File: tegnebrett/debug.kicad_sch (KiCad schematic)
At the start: 28 parts, among them J6 FPGA_Header_Pin, J9 FPGA_debug1, U1 XC7A100T-2FTG256I, U2 Oscillator 100MHz, U8 IS66WVH16M8DBLL-100B1LI1

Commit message: feat: add footprint for each capacitor
It's all 0805, 1206 or 1210 hand soldering variants.
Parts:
- C46, C47, C48, C49, C50, C51: footprint (none) -> Capacitor_SMD:C_0805_2012Metric_Pad1.18x1.45mm_HandSolder
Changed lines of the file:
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@@
 			)
 		)
-		(property "Footprint" ""
+		(property "Footprint" "Capacitor_SMD:C_0805_2012Metric_Pad1.18x1.45mm_HandSolder"
 			(at 133.0452 41.91 0)
 			(effects
@@
 			)
 		)
-		(property "Footprint" ""
+		(property "Footprint" "Capacitor_SMD:C_0805_2012Metric_Pad1.18x1.45mm_HandSolder"
 			(at 367.9952 85.09 0)
 			(effects
@@
 			)
 		)
-		(property "Footprint" ""
+		(property "Footprint" "Capacitor_SMD:C_0805_2012Metric_Pad1.18x1.45mm_HandSolder"
 			(at 63.1952 30.48 0)
 			(effects
@@
 			)
 		)
-		(property "Footprint" ""
+		(property "Footprint" "Capacitor_SMD:C_0805_2012Metric_Pad1.18x1.45mm_HandSolder"
 			(at 359.1052 85.09 0)
 			(effects
@@
 			)
 		)
-		(property "Footprint" ""
+		(property "Footprint" "Capacitor_SMD:C_0805_2012Metric_Pad1.18x1.45mm_HandSolder"
 			(at 375.6152 85.09 0)
 			(effects
@@
 			)
 		)
-		(property "Footprint" ""
+		(property "Footprint" "Capacitor_SMD:C_0805_2012Metric_Pad1.18x1.45mm_HandSolder"
 			(at 186.3852 138.43 0)
 			(effects

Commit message: feat: add footprint to resistors
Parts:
- R1, R2, R22, R3, R4, R5, R6, R64, R7, R8: footprint (none) -> Resistor_SMD:R_0805_2012Metric_Pad1.20x1.40mm_HandSolder
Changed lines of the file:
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@@
 			)
 		)
-		(property "Footprint" ""
+		(property "Footprint" "Resistor_SMD:R_0805_2012Metric_Pad1.20x1.40mm_HandSolder"
 			(at 120.142 74.93 90)
 			(effects
@@
 			)
 		)
-		(property "Footprint" ""
+		(property "Footprint" "Resistor_SMD:R_0805_2012Metric_Pad1.20x1.40mm_HandSolder"
 			(at 93.218 22.86 90)
 			(effects
@@
 			)
 		)
-		(property "Footprint" ""
+		(property "Footprint" "Resistor_SMD:R_0805_2012Metric_Pad1.20x1.40mm_HandSolder"
 			(at 207.772 175.26 90)
 			(effects
@@
 			)
 		)
-		(property "Footprint" ""
+		(property "Footprint" "Resistor_SMD:R_0805_2012Metric_Pad1.20x1.40mm_HandSolder"
 			(at 143.002 38.1 90)
 			(effects
@@
 			)
 		)
-		(property "Footprint" ""
+		(property "Footprint" "Resistor_SMD:R_0805_2012Metric_Pad1.20x1.40mm_HandSolder"
 			(at 113.792 74.93 90)
 			(effects
@@
 			)
 		)
-		(property "Footprint" ""
+		(property "Footprint" "Resistor_SMD:R_0805_2012Metric_Pad1.20x1.40mm_HandSolder"
 			(at 86.868 22.86 90)
 			(effects
@@
 			)
 		)
-		(property "Footprint" ""
+		(property "Footprint" "Resistor_SMD:R_0805_2012Metric_Pad1.20x1.40mm_HandSolder"
 			(at 174.752 38.1 90)
 			(effects
@@
 			)
 		)
-		(property "Footprint" ""
+		(property "Footprint" "Resistor_SMD:R_0805_2012Metric_Pad1.20x1.40mm_HandSolder"
 			(at 106.172 74.93 90)
 			(effects
@@
 			)
 		)
-		(property "Footprint" ""
+		(property "Footprint" "Resistor_SMD:R_0805_2012Metric_Pad1.20x1.40mm_HandSolder"
 			(at 200.152 175.26 90)
 			(effects
@@
 			)
 		)
-		(property "Footprint" ""
+		(property "Footprint" "Resistor_SMD:R_0805_2012Metric_Pad1.20x1.40mm_HandSolder"
 			(at 181.102 38.1 90)
 			(effects

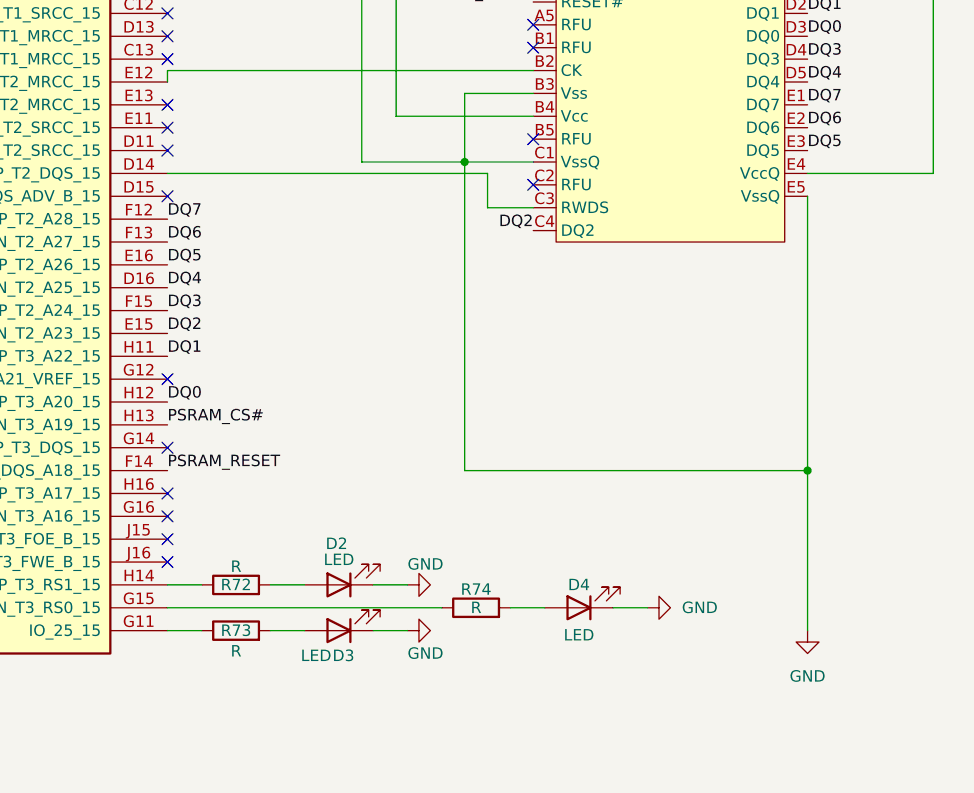
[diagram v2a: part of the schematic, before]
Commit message: refactor: remove some general bottuns from MCU
We have gone down from 9 buttons total to 6 buttons total.
One button is connected to the FPGA.
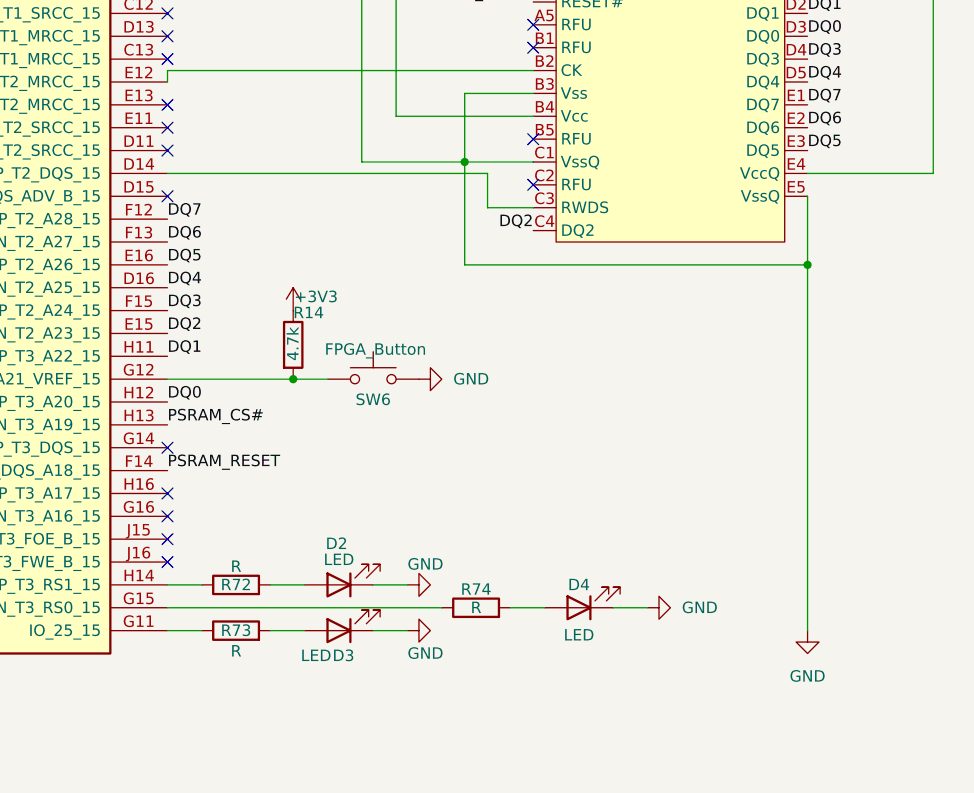
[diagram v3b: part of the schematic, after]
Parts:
- added R14: 4.7k, Resistor_SMD:R_0805_2012Metric_Pad1.20x1.40mm_HandSolder, symbol Device:R
- added SW6: FPGA_Button, symbol Switch:SW_Push
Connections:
- net +3V3: now also R14.1
- net GND: now also SW6.2
- net at U1.G12 (IO_L19N_T3_A21_VREF_15): now also R14.2, SW6.1
- no-connect marks 133 -> 132

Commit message: feat: add footprint to FPGA_debug
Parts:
- J9: footprint (none) -> Connector_PinHeader_2.54mm:PinHeader_2x07_P2.54mm_Vertical
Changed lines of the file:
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@@
 			)
 		)
-		(property "Footprint" ""
+		(property "Footprint" "Connector_PinHeader_2.54mm:PinHeader_2x07_P2.54mm_Vertical"
 			(at 106.68 21.59 0)
 			(effects

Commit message: feat: add and import footprints of trash buttons
These buttons are cheap and do the job fine.
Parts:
- SW6: footprint (none) -> tegnebrett_modules:SW_PS1024ALRED
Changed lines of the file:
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@@
 			)
 		)
-		(property "Footprint" ""
+		(property "Footprint" "tegnebrett_modules:SW_PS1024ALRED"
 			(at 342.9 139.7 0)
 			(effects

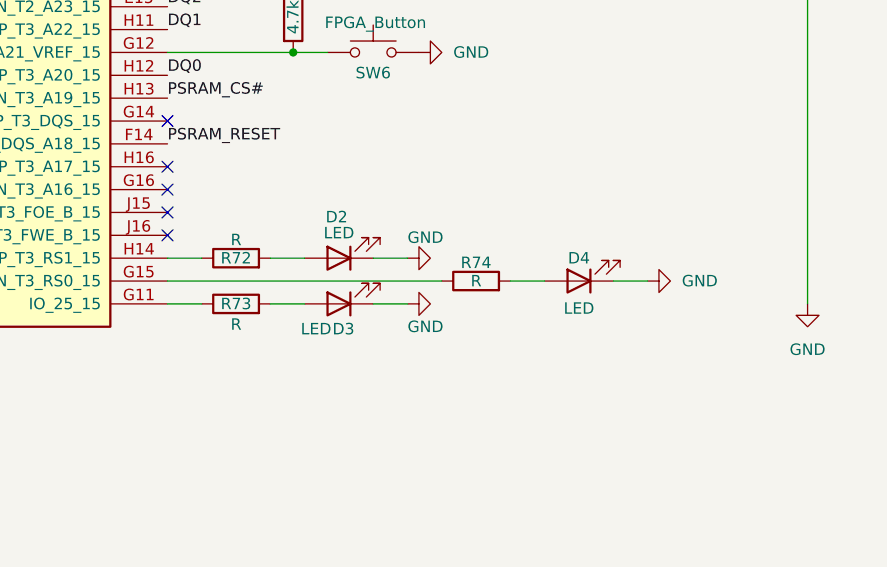
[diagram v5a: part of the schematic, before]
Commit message: refactor: remove unused LEDs
We have too many LEDs.
We're thinking two LEDs for the MCU and two LEDs for the FPGA.
Additionally have one Green LED at power supply to indicate that power
is on.
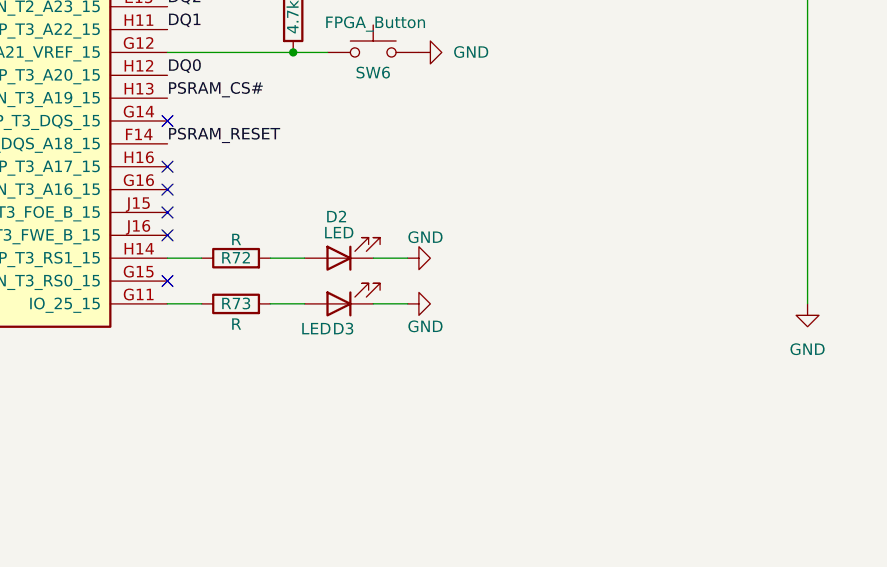
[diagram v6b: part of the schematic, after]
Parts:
- removed D4: LED, tegnebrett_modules:LED_J-SERIES_3030_CRW-M, symbol Device:LED
- removed R74: R, symbol Device:R
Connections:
- no-connect marks 132 -> 133
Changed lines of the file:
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@@
 	)
 	(no_connect
+		(at 320.04 170.18)
+	)
+	(no_connect
 		(at 218.44 106.68)
 	)
@@
 	(wire
 		(pts
-			(xy 369.57 170.18) (xy 373.38 170.18)
-		)
-		(stroke
-			(width 0)
-			(type default)
-		)
-	)
-	(wire
-		(pts
 			(xy 358.14 85.09) (xy 367.03 85.09)
 		)
@@
 	(wire
 		(pts
-			(xy 358.14 170.18) (xy 361.95 170.18)
-		)
-		(stroke
-			(width 0)
-			(type default)
-		)
-	)
-	(wire
-		(pts
 			(xy 100.33 132.08) (xy 102.87 132.08)
 		)
@@
 	(wire
 		(pts
-			(xy 320.04 170.18) (xy 350.52 170.18)
-		)
-		(stroke
-			(width 0)
-			(type default)
-		)
-	)
-	(wire
-		(pts
 			(xy 88.9 34.29) (xy 101.6 34.29)
 		)
@@
 	)
 	(symbol
-		(lib_id "Device:LED")
-		(at 365.76 170.18 180)
-		(unit 1)
-		(exclude_from_sim no)
-		(in_bom yes)
-		(on_board yes)
-		(dnp no)
-		(property "Reference" "D4"
-			(at 365.76 167.64 0)
-			(effects
-				(font
-					(size 1.27 1.27)
-				)
-			)
-		)
-		(property "Value" "LED"
-			(at 365.76 173.228 0)
-			(effects
-				(font
-					(size 1.27 1.27)
-				)
-			)
-		)
-		(property "Footprint" "tegnebrett_modules:LED_J-SERIES_3030_CRW-M"
-			(at 365.76 170.18 0)
-			(effects
-				(font
-					(size 1.27 1.27)
-				)
-				(hide yes)
-			)
-		)
-		(property "Datasheet" "~"
-			(at 365.76 170.18 0)
-			(effects
-				(font
-					(size 1.27 1.27)
-				)
-				(hide yes)
-			)
-		)
-		(property "Description" "Light emitting diode"
-			(at 365.76 170.18 0)
-			(effects
-				(font
-					(size 1.27 1.27)
-				)
-				(hide yes)
-			)
-		)
-		(property "Sim.Pins" "1=K 2=A"
-			(at 365.76 170.18 0)
-			(effects
-				(font
-					(size 1.27 1.27)
-				)
-				(hide yes)
-			)
-		)
-		(pin "2"
-		)
-		(pin "1"
-		)
-		(instances
-			(project "getting-started"
-				(path "/d9a31669-c5f1-42a7-9461-3df04b9a4e62/5e0df967-c6b5-4cdf-8fe6-93251df44e99"
-					(reference "D4")
-					(unit 1)
-				)
-			)
-		)
-	)
-	(symbol
 		(lib_id "power:GND")
 		(at 113.03 132.08 0)
@@
 	(symbol
 		(lib_id "Device:R")
-		(at 354.33 170.18 90)
-		(unit 1)
-		(exclude_from_sim no)
-		(in_bom yes)
-		(on_board yes)
-		(dnp no)
-		(property "Reference" "R74"
-			(at 354.33 168.148 90)
-			(effects
-				(font
-					(size 1.27 1.27)
-				)
-			)
-		)
-		(property "Value" "R"
-			(at 354.33 170.18 90)
-			(effects
-				(font
-					(size 1.27 1.27)
-				)
-			)
-		)
-		(property "Footprint" ""
-			(at 354.33 171.958 90)
-			(effects
-				(font
-					(size 1.27 1.27)
-				)
-				(hide yes)
-			)
-		)
-		(property "Datasheet" "~"
-			(at 354.33 170.18 0)
-			(effects
-				(font
-					(size 1.27 1.27)
-				)
-				(hide yes)
-			)
-		)
-		(property "Description" "Resistor"
-			(at 354.33 170.18 0)
-			(effects
-				(font
-					(size 1.27 1.27)
-				)
-				(hide yes)
-			)
-		)
-		(pin "1"
-		)
-		(pin "2"
-		)
-		(instances
-			(project "getting-started"
-				(path "/d9a31669-c5f1-42a7-9461-3df04b9a4e62/5e0df967-c6b5-4cdf-8fe6-93251df44e99"
-					(reference "R74")
-					(unit 1)
-				)
-			)
-		)
-	)
-	(symbol
-		(lib_id "Device:R")
 		(at 85.09 22.86 180)
 		(unit 1)
@@
 					(unit 1)
 				)
-			)
-		)
-	)
-	(symbol
-		(lib_id "power:GND")
-		(at 373.38 170.18 90)
-		(unit 1)
-		(exclude_from_sim no)
-		(in_bom yes)
-		(on_board yes)
-		(dnp no)
-		(fields_autoplaced yes)
-		(property "Reference" "#PWR084"
-			(at 379.73 170.18 0)
-			(effects
-				(font
-					(size 1.27 1.27)
-				)
-				(hide yes)
-			)
-		)
-		(property "Value" "GND"
-			(at 377.19 170.1799 90)
-			(effects
-				(font
-					(size 1.27 1.27)
-				)
-				(justify right)
-			)
-		)
-		(property "Footprint" ""
-			(at 373.38 170.18 0)
-			(effects
-				(font
-					(size 1.27 1.27)
-				)
-				(hide yes)
-			)
-		)
-		(property "Datasheet" ""
-			(at 373.38 170.18 0)
-			(effects
-				(font
-					(size 1.27 1.27)
-				)
-				(hide yes)
-			)
-		)
-		(property "Description" "Power symbol creates a global label with name \"GND\" , ground"
-			(at 373.38 170.18 0)
-			(effects
-				(font
-					(size 1.27 1.27)
-				)
-				(hide yes)
-			)
-		)
-		(pin "1"
-		)
-		(instances
-			(project "getting-started"
-				(path "/d9a31669-c5f1-42a7-9461-3df04b9a4e62/5e0df967-c6b5-4cdf-8fe6-93251df44e99"
-					(reference "#PWR084")
-					(unit 1)
-				)

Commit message: refactor: use new LED variants.
These have a supply voltage of 2V, and they have a current of 5mA.
These are nice numbers which gives a required resistance of 260 Ohm,
assuming a supply voltage of 3.3V

We're using 270 Ohms though, as 260 is not standard.
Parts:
- D2, D3: footprint tegnebrett_modules:LED_J-SERIES_3030_CRW-M -> tegnebrett_modules:LED_LTST-C193KGKT-5A_LTO-M
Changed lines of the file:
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@@
 			)
 		)
-		(property "Footprint" "tegnebrett_modules:LED_J-SERIES_3030_CRW-M"
+		(property "Footprint" "tegnebrett_modules:LED_LTST-C193KGKT-5A_LTO-M"
 			(at 339.09 167.64 0)
 			(effects
@@
 			)
 		)
-		(property "Footprint" "tegnebrett_modules:LED_J-SERIES_3030_CRW-M"
+		(property "Footprint" "tegnebrett_modules:LED_LTST-C193KGKT-5A_LTO-M"
 			(at 339.09 172.72 0)
 			(effects

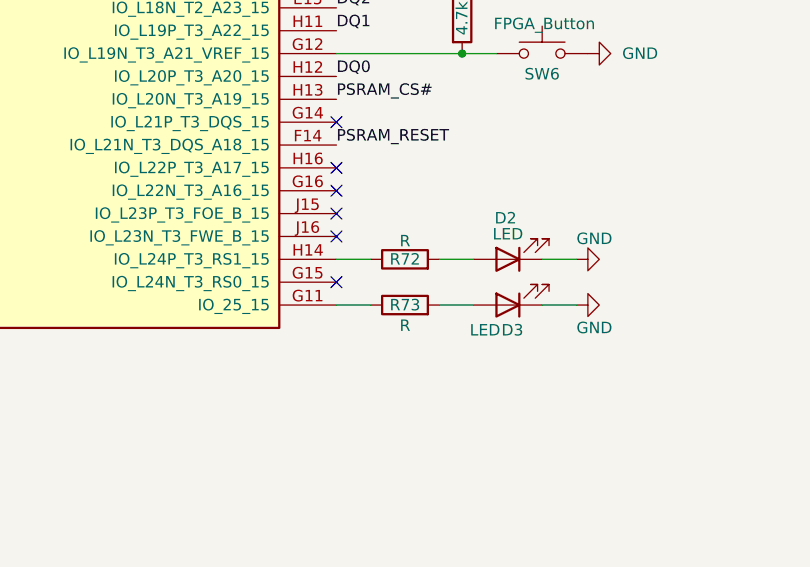
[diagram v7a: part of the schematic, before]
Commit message: feat: add LED to 3.3V from power supply, and set resistors to 270ohm.
Additionally add footprints to these resistors which *did not* yet have
a footprint (because their resistor values were not determined yet).
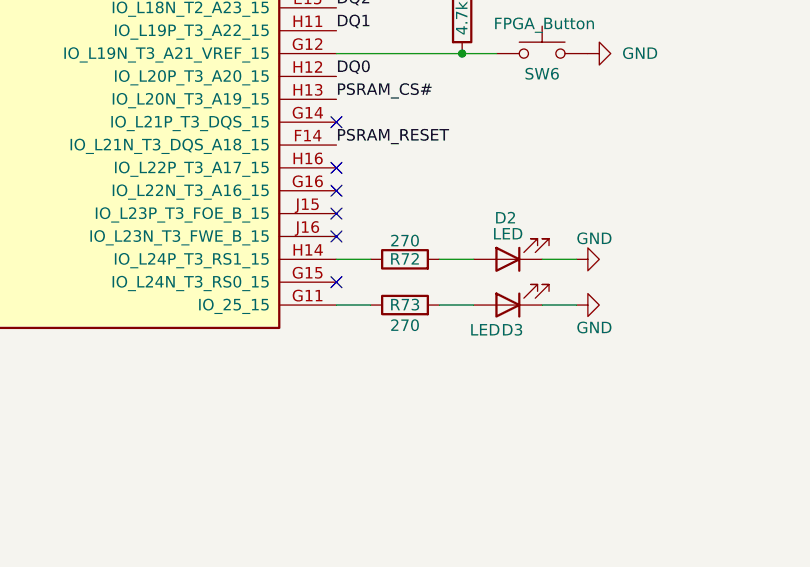
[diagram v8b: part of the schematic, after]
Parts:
- R72, R73: value R -> 270; footprint (none) -> Resistor_SMD:R_0805_2012Metric_Pad1.20x1.40mm_HandSolder
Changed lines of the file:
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@@
 			)
 		)
-		(property "Value" "R"
+		(property "Value" "270"
 			(at 327.66 175.006 90)
 			(effects
@@
 			)
 		)
-		(property "Footprint" ""
+		(property "Footprint" "Resistor_SMD:R_0805_2012Metric_Pad1.20x1.40mm_HandSolder"
 			(at 327.66 174.498 90)
 			(effects
@@
 			)
 		)
-		(property "Value" "R"
+		(property "Value" "270"
 			(at 327.66 165.608 90)
 			(effects
@@
 			)
 		)
-		(property "Footprint" ""
+		(property "Footprint" "Resistor_SMD:R_0805_2012Metric_Pad1.20x1.40mm_HandSolder"
 			(at 327.66 169.418 90)
 			(effects
